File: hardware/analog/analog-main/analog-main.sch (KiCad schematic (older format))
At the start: 1 part, among them U1 OPA549_KVC_11

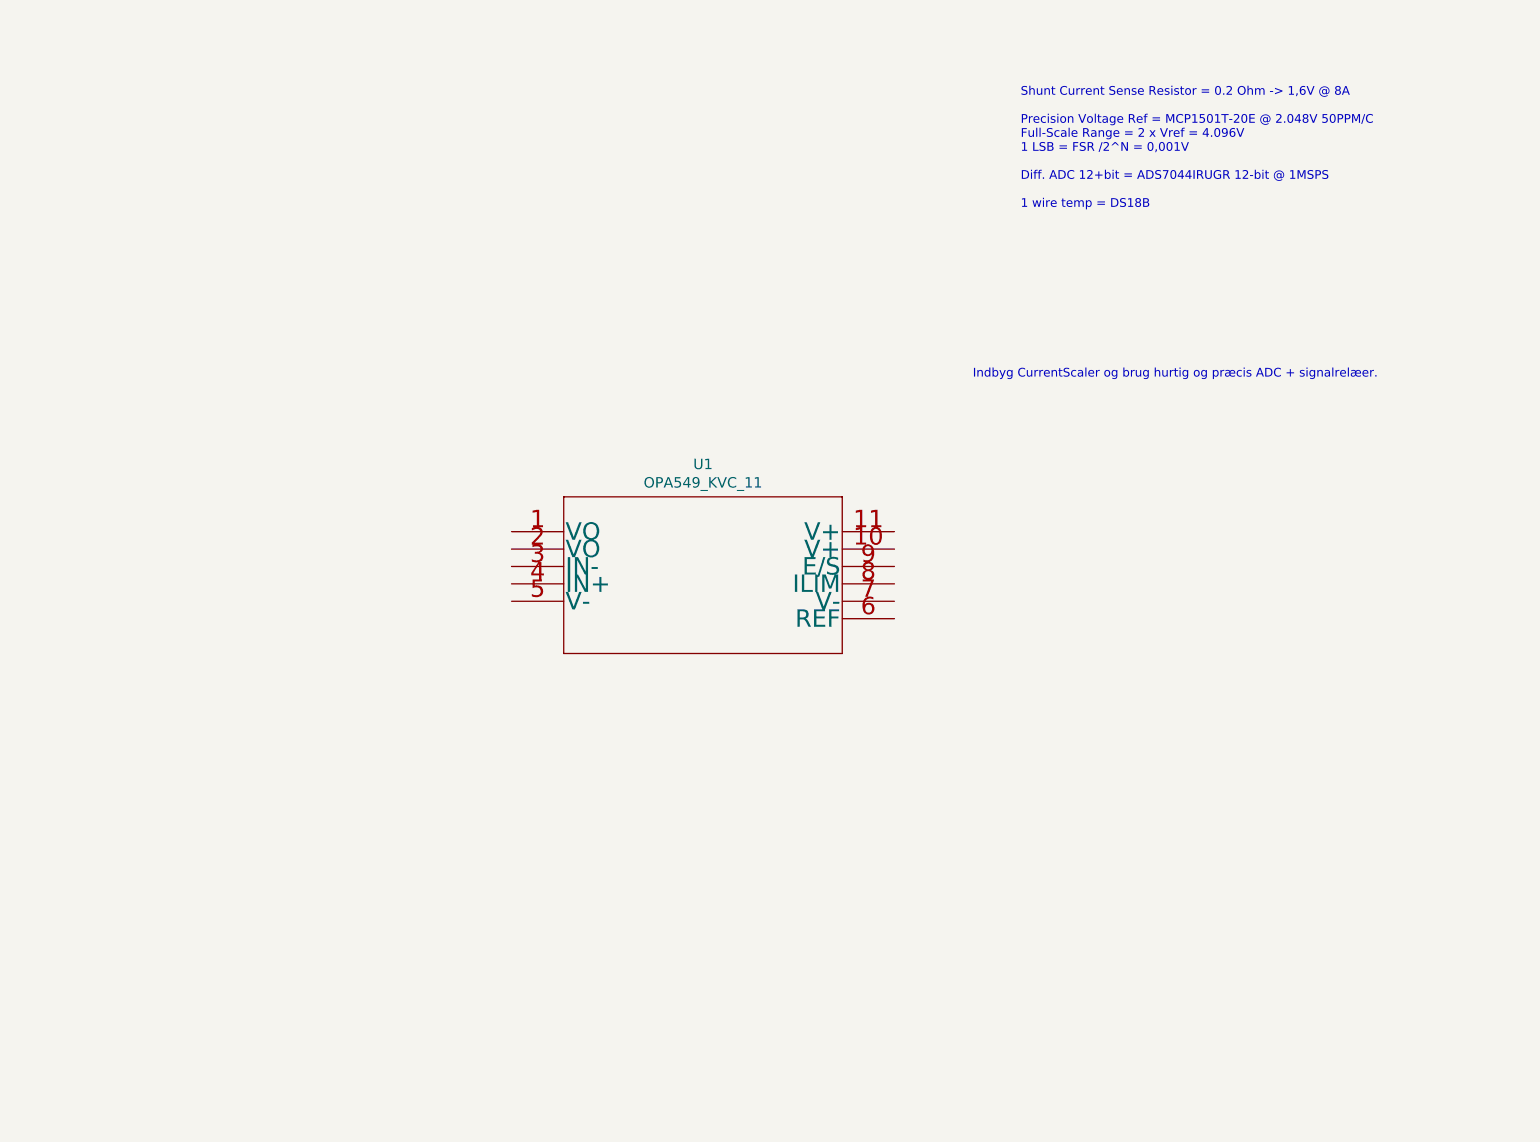
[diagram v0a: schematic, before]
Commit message: Started work on Analog Main (Power Supply) board
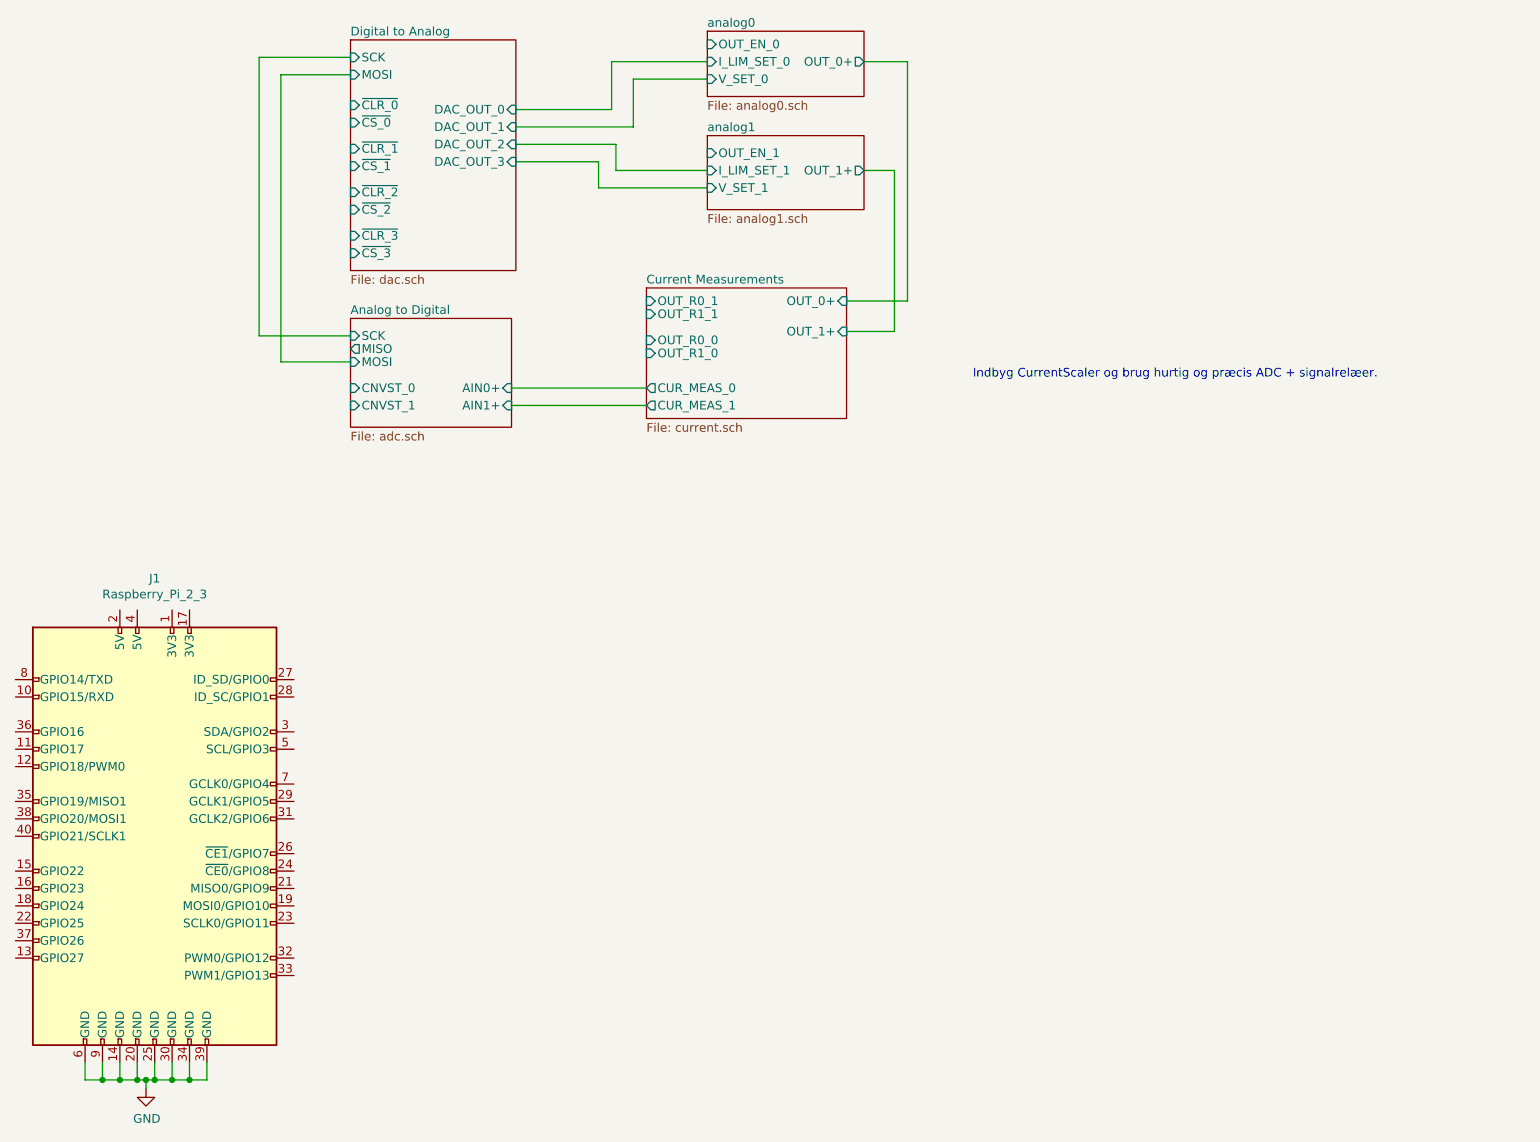
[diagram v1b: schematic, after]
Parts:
- removed U1: OPA549_KVC_11, Package_TO_SOT_THT:TO-220-11_P3.4x5.08mm_StaggerOdd_Lead4.85mm_Vertical, symbol symbols:OPA549_KVC_11
- added J1: Raspberry_Pi_2_3, Module:Raspberry_Pi_Zero_Socketed_THT_FaceDown_MountingHoles, symbol Connector:Raspberry_Pi_2_3
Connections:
- new net GND: J1.14 (GND), J1.20 (GND), J1.25 (GND), J1.30 (GND), J1.34 (GND), J1.39 (GND), J1.6 (GND), J1.9 (GND)
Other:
- note removed: "Shunt Current Sense Resistor = 0.2 Ohm -> 1,6V @ 8A\n\nPrecision Voltage Ref = MCP1501T-20E @ 2.048V 50PPM/C\nFull-Scale Range = 2 x Vref = 4.096V\n1 LSB = FSR /2^N = 0,001V\n\nDiff. ADC 12+bit = ADS7044IRUGR 12-bit @ 1MSPS\n\n1 wire temp = DS18B"
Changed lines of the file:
@@
 $Descr A4 11693 8268
 encoding utf-8
-Sheet 1 1
+Sheet 1 6
 Title ""
 Date ""
@@
 Comment4 ""
 $EndDescr
+Text Notes 6475 2825 0    50   ~ 0
+Indbyg CurrentScaler og brug hurtig og præcis ADC + signalrelæer.
+$Sheet
+S 4950 825  900  375
+U 5E862B85
+F0 "analog0" 50
+F1 "analog0.sch" 50
+F2 "OUT_EN_0" I L 4950 900 50
+F3 "I_LIM_SET_0" I L 4950 1000 50
+F4 "V_SET_0" I L 4950 1100 50
+F5 "OUT_0+" O R 5850 1000 50
+$EndSheet
+$Sheet
+S 2900 875  950  1325
+U 5E86D055
+F0 "Digital to Analog" 50
+F1 "dac.sch" 50
+F2 "SCK" I L 2900 975 50
+F3 "MOSI" I L 2900 1075 50
+F4 "~CLR_0" I L 2900 1250 50
+F5 "~CS_0" I L 2900 1350 50
+F6 "DAC_OUT_0" I R 3850 1275 50
+F7 "~CLR_1" I L 2900 1500 50
+F8 "~CS_1" I L 2900 1600 50
+F9 "DAC_OUT_1" I R 3850 1375 50
+F10 "~CLR_2" I L 2900 1750 50
+F11 "~CS_2" I L 2900 1850 50
+F12 "DAC_OUT_2" I R 3850 1475 50
+F13 "~CLR_3" I L 2900 2000 50
+F14 "~CS_3" I L 2900 2100 50
+F15 "DAC_OUT_3" I R 3850 1575 50
+$EndSheet
+$Sheet
+S 2900 2475 925  625
+U 5E86F885
+F0 "Analog to Digital" 50
+F1 "adc.sch" 50
+F2 "SCK" I L 2900 2575 50
+F3 "MISO" O L 2900 2650 50
+F4 "CNVST_0" I L 2900 2875 50
+F5 "AIN0+" I R 3825 2875 50
+F7 "CNVST_1" I L 2900 2975 50
+F8 "AIN1+" I R 3825 2975 50
+F10 "MOSI" I L 2900 2725 50
+$EndSheet
 $Comp
-L symbols:OPA549_KVC_11 U1
-U 1 1 5DF29E17
-P 3825 3700
-F 0 "U1" H 4925 4087 60  0000 C CNN
-F 1 "OPA549_KVC_11" H 4925 3981 60  0000 C CNN
-F 2 "Package_TO_SOT_THT:TO-220-11_P3.4x5.08mm_StaggerOdd_Lead4.85mm_Vertical" H 4925 3940 60  0001 C CNN
-F 3 "" H 3825 3700 60  0000 C CNN
-	1    3825 3700
+L Connector:Raspberry_Pi_2_3 J1
+U 1 1 5E86FE68
+P 1775 5450
+F 0 "J1" H 1775 6931 50  0000 C CNN
+F 1 "Raspberry_Pi_2_3" H 1775 6840 50  0000 C CNN
+F 2 "Module:Raspberry_Pi_Zero_Socketed_THT_FaceDown_MountingHoles" H 1775 5450 50  0001 C CNN
+F 3 "https://www.raspberrypi.org/documentation/hardware/raspberrypi/schematics/rpi_SCH_3bplus_1p0_reduced.pdf" H 1775 5450 50  0001 C CNN
+	1    1775 5450
 	1    0    0    -1
 $EndComp
-Text Notes 6750 1850 0    50   ~ 0
-Shunt Current Sense Resistor = 0.2 Ohm -> 1,6V @ 8A\n\nPrecision Voltage Ref = MCP1501T-20E @ 2.048V 50PPM/C\nFull-Scale Range = 2 x Vref = 4.096V\n1 LSB = FSR /2^N = 0,001V\n\nDiff. ADC 12+bit = ADS7044IRUGR 12-bit @ 1MSPS\n\n1 wire temp = DS18B
-Text Notes 6475 2825 0    50   ~ 0
-Indbyg CurrentScaler og brug hurtig og præcis ADC + signalrelæer.
+$Sheet
+S 4950 1425 900  425
+U 5E975E66
+F0 "analog1" 50
+F1 "analog1.sch" 50
+F2 "OUT_EN_1" I L 4950 1525 50
+F3 "I_LIM_SET_1" I L 4950 1625 50
+F4 "V_SET_1" I L 4950 1725 50
+F5 "OUT_1+" O R 5850 1625 50
+$EndSheet
+Wire Wire Line
+	4950 1000 4400 1000
+Wire Wire Line
+	4400 1000 4400 1275
+Wire Wire Line
+	4400 1275 3850 1275
+Wire Wire Line
+	3850 1375 4525 1375
+Wire Wire Line
+	4525 1375 4525 1100
+Wire Wire Line
+	4525 1100 4950 1100
+Wire Wire Line
+	4950 1625 4425 1625
+Wire Wire Line
+	4425 1625 4425 1475
+Wire Wire Line
+	4425 1475 3850 1475
+Wire Wire Line
+	3850 1575 4325 1575
+Wire Wire Line
+	4325 1575 4325 1725
+Wire Wire Line
+	4325 1725 4950 1725
+Wire Wire Line
+	2900 975  2375 975
+Wire Wire Line
+	2375 975  2375 2575
+Wire Wire Line
+	2375 2575 2900 2575
+Wire Wire Line
+	2900 2725 2500 2725
+Wire Wire Line
+	2500 2725 2500 1075
+Wire Wire Line
+	2500 1075 2900 1075
+$Comp
+L power:GND #PWR01
+U 1 1 5EB04124
+P 1725 6900
+F 0 "#PWR01" H 1725 6650 50  0001 C CNN
+F 1 "GND" H 1730 6727 50  0000 C CNN
+F 2 "" H 1725 6900 50  0001 C CNN
+F 3 "" H 1725 6900 50  0001 C CNN
+	1    1725 6900
+	1    0    0    -1
+$EndComp
+Wire Wire Line
+	1725 6900 1725 6850
+Wire Wire Line
+	1725 6850 1775 6850
+Wire Wire Line
+	2075 6850 2075 6750
+Wire Wire Line
+	1975 6750 1975 6850
+Connection ~ 1975 6850
+Wire Wire Line
+	1975 6850 2075 6850
+Wire Wire Line
+	1725 6850 1675 6850
+Wire Wire Line
+	1375 6850 1375 6750
+Connection ~ 1725 6850
+Wire Wire Line
+	1475 6750 1475 6850
+Connection ~ 1475 6850
+Wire Wire Line
+	1475 6850 1375 6850
+Wire Wire Line
+	1575 6750 1575 6850
+Connection ~ 1575 6850
+Wire Wire Line
+	1575 6850 1475 6850
+Wire Wire Line
+	1675 6750 1675 6850
+Connection ~ 1675 6850
+Wire Wire Line
+	1675 6850 1575 6850
+Wire Wire Line
+	1775 6750 1775 6850
+Connection ~ 1775 6850
+Wire Wire Line
+	1775 6850 1875 6850
+Wire Wire Line
+	1875 6750 1875 6850
+Connection ~ 1875 6850
+Wire Wire Line
+	1875 6850 1975 6850
+Wire Wire Line
+	5850 1000 6100 1000
+Wire Wire Line
+	6100 1000 6100 2375
+$Sheet
+S 4600 2300 1150 750
+U 5EB10C4C
+F0 "Current Measurements" 50
+F1 "current.sch" 50
+F2 "OUT_0+" I R 5750 2375 50
+F3 "OUT_1+" I R 5750 2550 50
+F4 "OUT_R0_1" I L 4600 2375 50
+F5 "CUR_MEAS_0" O L 4600 2875 50
+F6 "OUT_R1_1" I L 4600 2450 50
+F7 "OUT_R0_0" I L 4600 2600 50
+F8 "OUT_R1_0" I L 4600 2675 50
+F9 "CUR_MEAS_1" O L 4600 2975 50
+$EndSheet
+Wire Wire Line
+	6025 2550 6025 1625
+Wire Wire Line
+	6025 1625 5850 1625
+Wire Wire Line
+	3825 2875 4600 2875
+Wire Wire Line
+	4600 2975 3825 2975
+Wire Wire Line
+	5750 2375 6100 2375
+Wire Wire Line
+	5750 2550 6025 2550
 $EndSCHEMATC

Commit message: Sorry future me
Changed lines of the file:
@@
 $Descr A4 11693 8268
 encoding utf-8
-Sheet 1 6
+Sheet 1 7
 Title ""
 Date ""
@@
 Wire Wire Line
 	5750 2550 6025 2550
+$Sheet
+S 4525 3700 1075 1425
+U 5EBAB32F
+F0 "AC2DC" 50
+F1 "ac2dc.sch" 50
+$EndSheet
 $EndSCHEMATC
